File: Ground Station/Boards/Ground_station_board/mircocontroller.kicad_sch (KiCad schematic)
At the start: 30 parts, among them J3 USB_B_Micro, J4 SWD JST PH, U4 STM32H562RGT6, Y2 12MHz

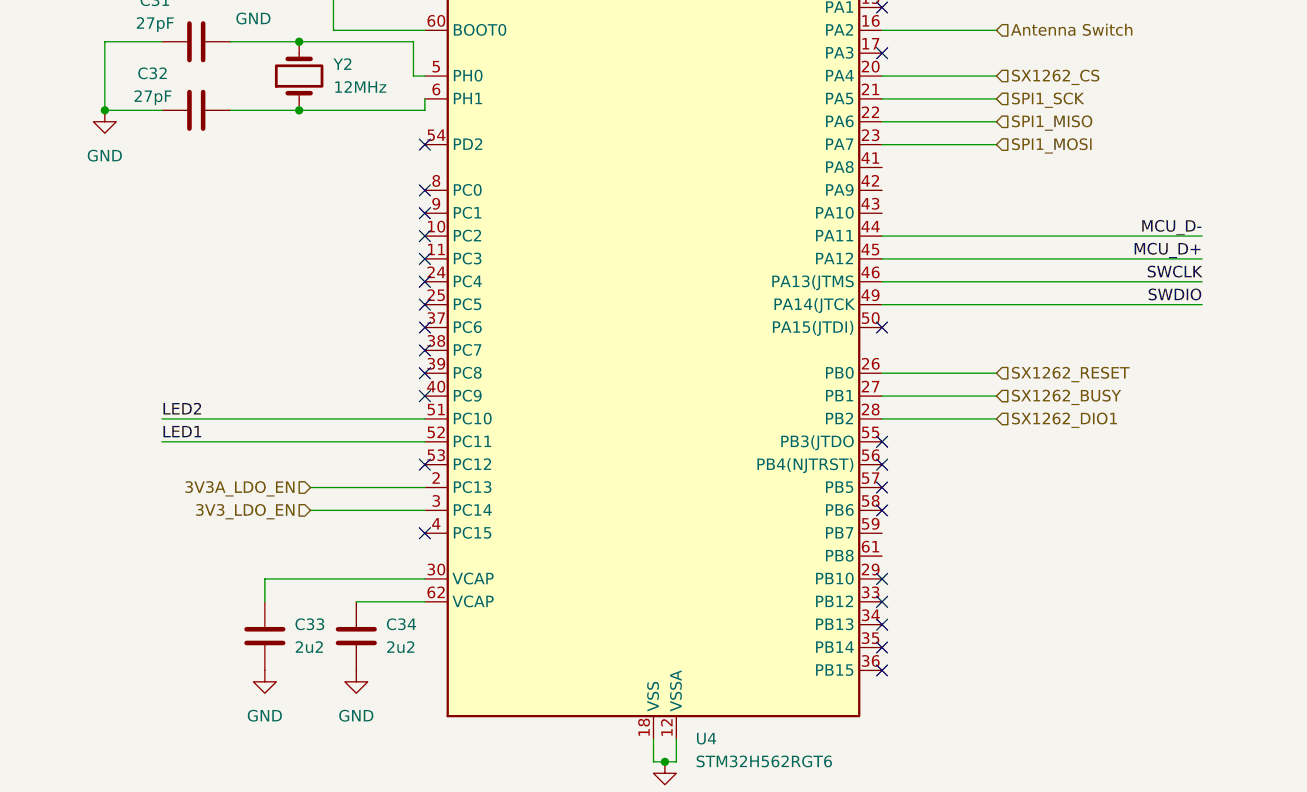
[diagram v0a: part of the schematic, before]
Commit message: via stitching added to gs board, need fencing before review
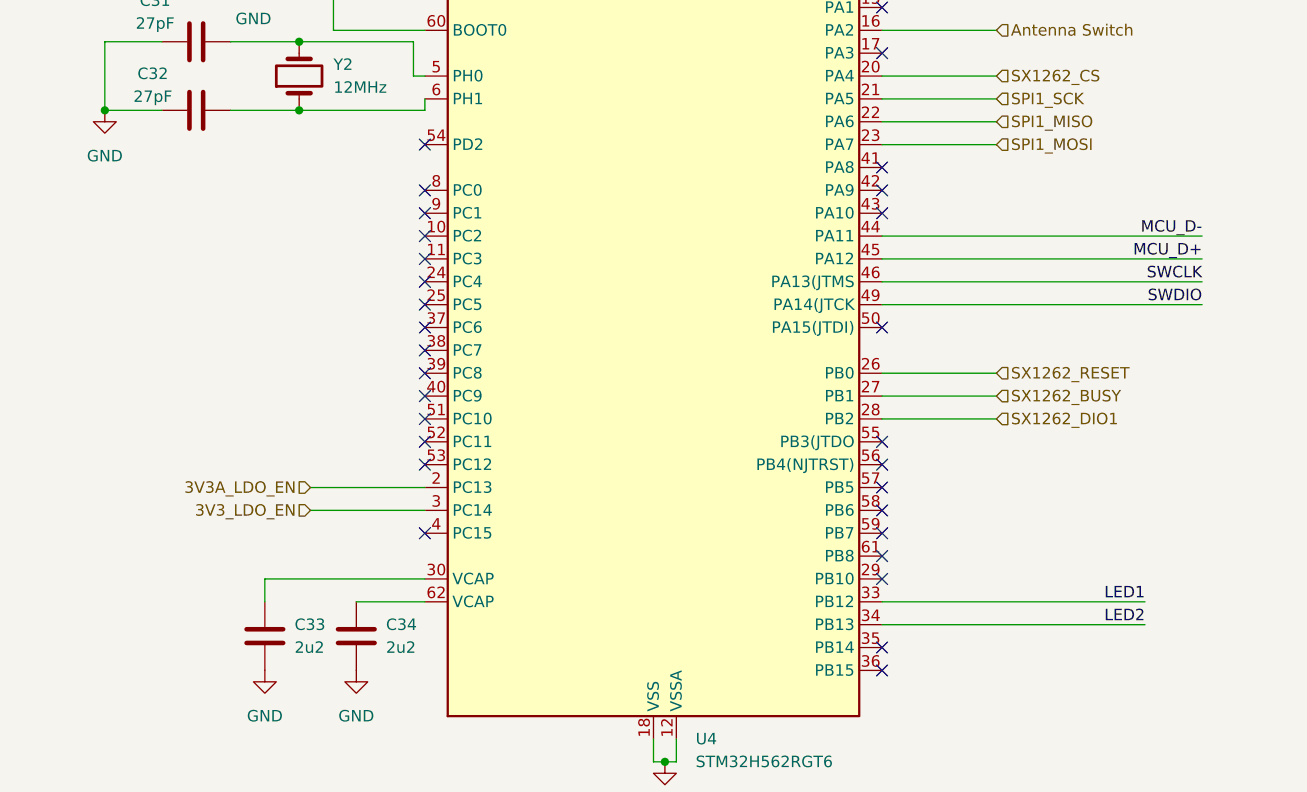
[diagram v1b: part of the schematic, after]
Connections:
- net LED1: now also U4.33 (PB12); no longer U4.52 (PC11)
- net LED2: now also U4.34 (PB13); no longer U4.51 (PC10)
- no-connect marks 29 -> 34
